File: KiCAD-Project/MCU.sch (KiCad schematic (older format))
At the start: 43 parts, among them J301 GPIOs, J302 JTAG/SW, U301 CY8C6244AZI-S4D92, U302 MCP9700AT-HTT, U303 MCP9700AT-HTT, Y301 32MHz

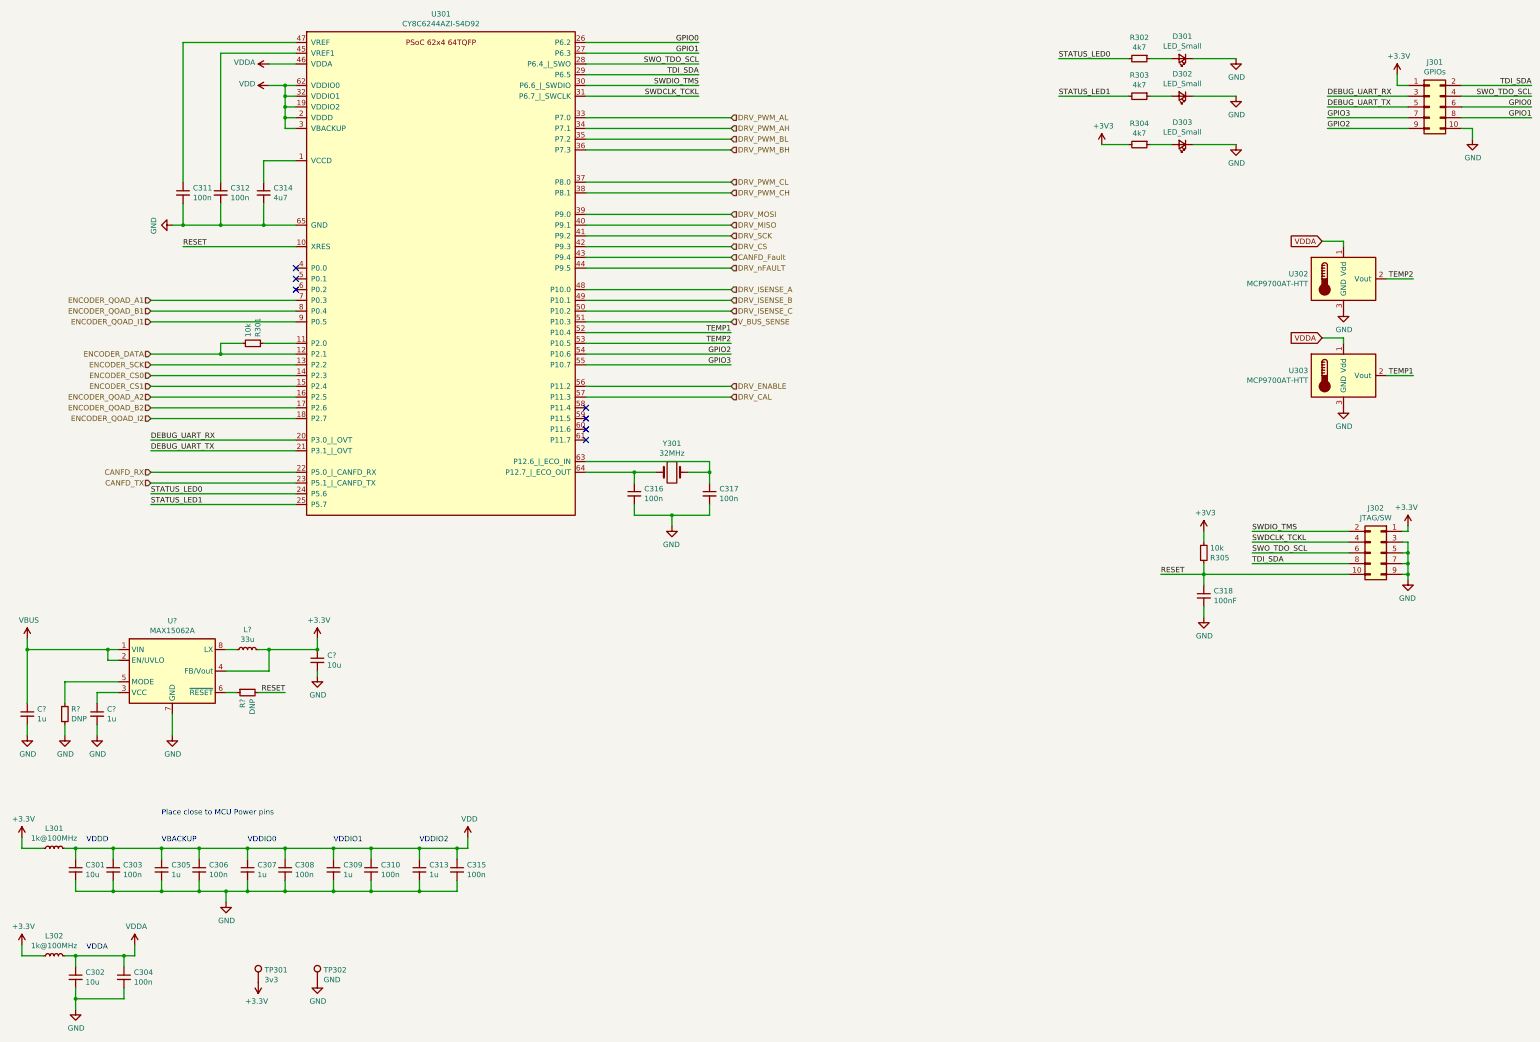
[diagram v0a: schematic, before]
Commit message: Schamtic package assigned
Package assigned, added two 100nF C's for temp sensors
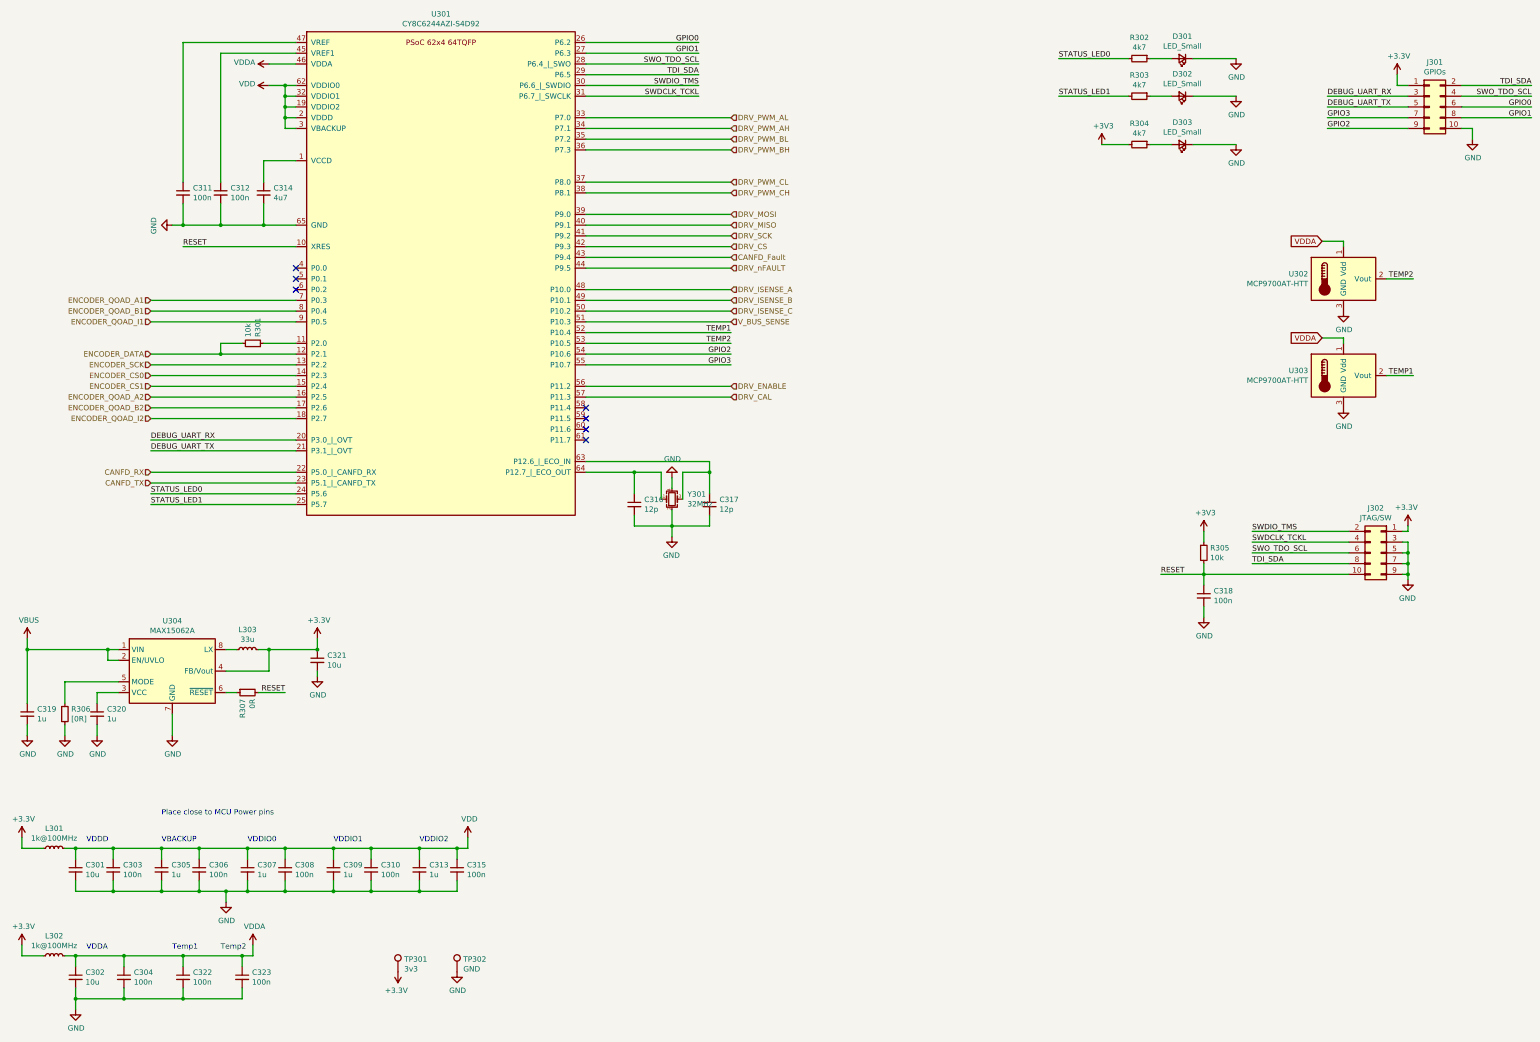
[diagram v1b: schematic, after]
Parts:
- removed Y301: 32MHz, symbol Device:Crystal
- added C322, C323: 100n, Capacitor_SMD:C_0603_1608Metric, symbol Device:C_Small
- added Y301: 32MHz, Crystal:Crystal_SMD_3225-4Pin_3.2x2.5mm_HandSoldering, symbol Device:Crystal_GND24_Small
- C301, C302: footprint (none) -> Capacitor_SMD:C_1206_3216Metric
- C303, C304, C305, C306, C307, C308, C309, C310, C311, C312, C313, C314, C315: footprint (none) -> Capacitor_SMD:C_0603_1608Metric
- C316, C317: value 100n -> 12p; footprint (none) -> Capacitor_SMD:C_0603_1608Metric
- C318: value 100nF -> 100n; footprint (none) -> Capacitor_SMD:C_0603_1608Metric
- C319, C320: renamed from C?; footprint (none) -> Capacitor_SMD:C_0603_1608Metric
- C321: renamed from C?; footprint (none) -> Capacitor_SMD:C_1206_3216Metric
- D301, D302, D303: footprint (none) -> LED_SMD:LED_0603_1608Metric
- J301: footprint (none) -> Connector_PinSocket_2.54mm:PinSocket_2x05_P2.54mm_Vertical
- J302: footprint (none) -> Connector_PinSocket_2.00mm:PinSocket_2x05_P2.00mm_Vertical_SMD
- L301, L302: footprint (none) -> Inductor_SMD:L_0603_1608Metric
- L303: renamed from L?; footprint (none) -> Inductor_SMD:L_1210_3225Metric
- R301, R302, R303, R304, R305: footprint (none) -> Resistor_SMD:R_0603_1608Metric
- R306: renamed from R?; value DNP -> [0R]; footprint (none) -> Resistor_SMD:R_0603_1608Metric
- R307: renamed from R?; value DNP -> 0R; footprint (none) -> Resistor_SMD:R_0603_1608Metric
- TP301: footprint (none) -> TestPoint:TestPoint_Pad_D2.0mm
- TP302: footprint (none) -> Connector_PinHeader_2.54mm:PinHeader_1x01_P2.54mm_Vertical
- U301: footprint (none) -> Package_DFN_QFN:Texas_S-PVQFN-N64_EP4.25x4.25mm_ThermalVias
- gave numbers to parts that had none: 1
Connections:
- net +3V3: now also R305.1; no longer R305.2
- net GND: now also C322.2, C323.2, Y301.2, Y301.4
- net RESET: now also R305.2; no longer R305.1
- net VDDA: now also C322.1, C323.1
- net at C317.1, U301.63 (P12.6_|_ECO_IN): now also Y301.3
- net at C316.1, U301.64 (P12.7_|_ECO_OUT): now also Y301.1
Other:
- note added: "Temp1"
- note added: "Temp2"
- moved on the sheet: C316, C317, TP301, TP302

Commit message: pcb draft
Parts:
- removed C319, C320: 1u, Capacitor_SMD:C_0603_1608Metric, symbol Device:C_Small
- removed C321: 10u, Capacitor_SMD:C_1206_3216Metric, symbol Device:C_Small
- removed L303: 33u, Inductor_SMD:L_1210_3225Metric, symbol Device:L_Small
- removed U304: MAX15062A, Package_DFN_QFN:DFN-8_2x2mm_P0.5mm, symbol Regulator_Switching:MAX15062A
- J301: footprint Connector_PinSocket_2.54mm:PinSocket_2x05_P2.54mm_Vertical -> Connector_PinHeader_2.54mm:PinHeader_2x05_P2.54mm_Vertical_SMD
- J302: footprint Connector_PinSocket_2.00mm:PinSocket_2x05_P2.00mm_Vertical_SMD -> Connector_PinHeader_2.00mm:PinHeader_2x05_P2.00mm_Vertical_SMD
- R306: value [0R] -> 4k7
- R307: value 0R -> 4k7
- Y301: footprint Crystal:Crystal_SMD_3225-4Pin_3.2x2.5mm_HandSoldering -> Crystal:Crystal_SMD_3225-4Pin_3.2x2.5mm
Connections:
- net +3V3: now also R306.1, R307.1
- net DEBUG_UART_RX: now also J301.7 (Pin_7); no longer J301.3 (Pin_3)
- net DEBUG_UART_TX: now also J301.9 (Pin_9); no longer J301.5 (Pin_5)
- net GND: no longer R306.2
- net GPIO0: now also J301.2 (Pin_2); no longer J301.6 (Pin_6)
- net GPIO1: now also J301.4 (Pin_4); no longer J301.8 (Pin_8)
- net GPIO2: now also J301.5 (Pin_5); no longer J301.9 (Pin_9)
- net GPIO3: now also J301.3 (Pin_3); no longer J301.7 (Pin_7)
- net RESET: no longer R307.2
- net SWO_TDO_SCL: now also J301.6 (Pin_6), R306.2; no longer J301.4 (Pin_4)
- net TDI_SDA: now also J301.8 (Pin_8), R307.2; no longer J301.2 (Pin_2)
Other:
- moved on the sheet: J301, U302, U303

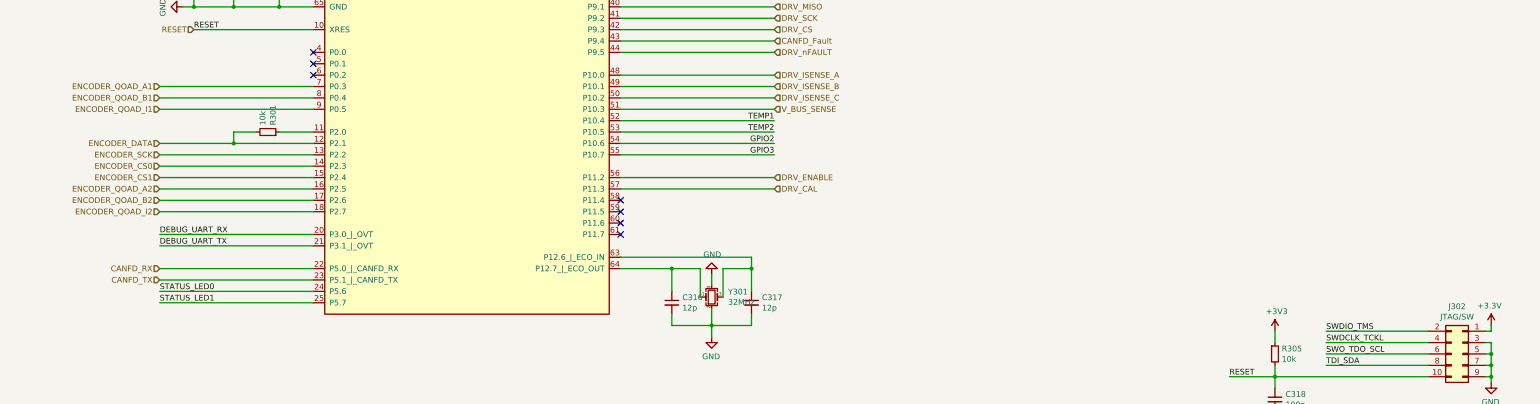
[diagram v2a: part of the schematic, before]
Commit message: layout redesign started
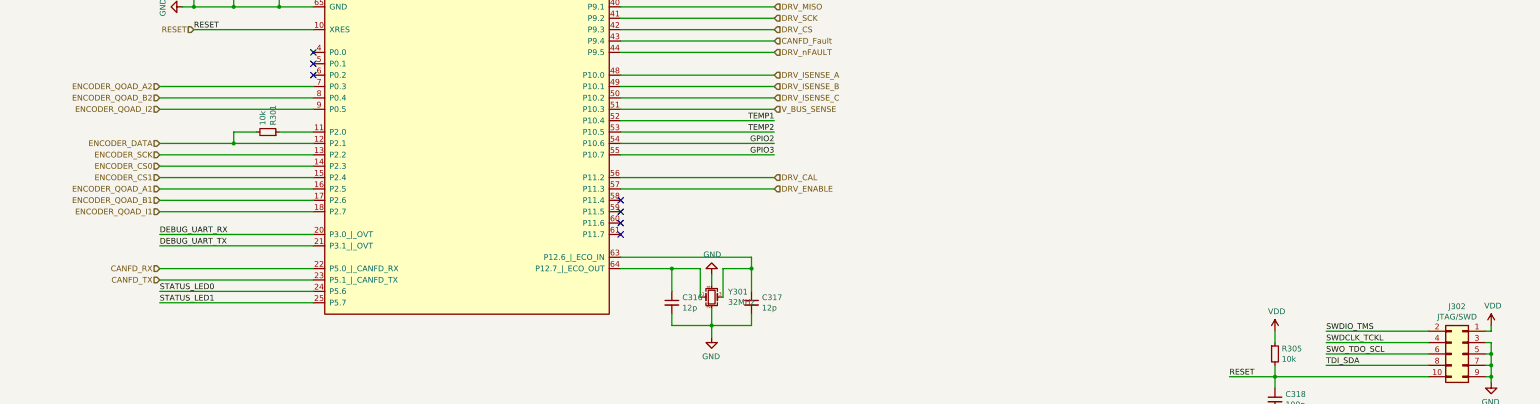
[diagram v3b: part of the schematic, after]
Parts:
- C301, C302: footprint Capacitor_SMD:C_1206_3216Metric -> Capacitor_SMD:C_0603_1608Metric
- J302: value JTAG/SW -> JTAG/SWD; footprint Connector_PinHeader_2.00mm:PinHeader_2x05_P2.00mm_Vertical_SMD -> Connector_PinHeader_1.27mm:PinHeader_2x05_P1.27mm_Vertical_SMD
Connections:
- net +3V3: no longer J302.1 (Pin_1), R305.1
- net DRV_CAL: now also U301.56 (P11.2); no longer U301.57 (P11.3)
- net DRV_ENABLE: now also U301.57 (P11.3); no longer U301.56 (P11.2)
- net ENCODER_QOAD_A1: now also U301.16 (P2.5); no longer U301.7 (P0.3)
- net ENCODER_QOAD_A2: now also U301.7 (P0.3); no longer U301.16 (P2.5)
- net ENCODER_QOAD_B1: now also U301.17 (P2.6); no longer U301.8 (P0.4)
- net ENCODER_QOAD_B2: now also U301.8 (P0.4); no longer U301.17 (P2.6)
- net ENCODER_QOAD_I1: now also U301.18 (P2.7); no longer U301.9 (P0.5)
- net ENCODER_QOAD_I2: now also U301.9 (P0.5); no longer U301.18 (P2.7)
- net VDD: now also J302.1 (Pin_1), R305.1
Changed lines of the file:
@@
 	11600 5950 12000 5950
-$Comp
-L power:+3V3 #PWR?
-U 1 1 60CAF38E
-P 12000 5550
-AR Path="/60CAF38E" Ref="#PWR?"  Part="1"
-AR Path="/60AF747C/60CAF38E" Ref="#PWR0318"  Part="1"
-F 0 "#PWR0318" H 12000 5400 50  0001 C CNN
-F 1 "+3V3" H 12015 5723 50  0000 C CNN
-F 2 "" H 12000 5550 50  0001 C CNN
-F 3 "" H 12000 5550 50  0001 C CNN
-	1    12000 5550
-	1    0    0    -1
-$EndComp
 $Comp
 L power:GND #PWR?
@@
 AR Path="/60AF747C/60CEE033" Ref="J302"  Part="1"
 F 0 "J302" H 13700 6167 50  0000 C CNN
-F 1 "JTAG/SW" H 13700 6076 50  0000 C CNN
-F 2 "Connector_PinHeader_2.00mm:PinHeader_2x05_P2.00mm_Vertical_SMD" H 13650 5750 50  0001 C CNN
+F 1 "JTAG/SWD" H 13700 6076 50  0000 C CNN
+F 2 "Connector_PinHeader_1.27mm:PinHeader_2x05_P1.27mm_Vertical_SMD" H 13650 5750 50  0001 C CNN
 F 3 "~" H 13650 5750 50  0001 C CNN
 	1    13650 5750
-	-1   0    0    -1
-$EndComp
-$Comp
-L power:+3.3V #PWR?
-U 1 1 60CEE03B
-P 13900 5500
-AR Path="/60CEE03B" Ref="#PWR?"  Part="1"
-AR Path="/60AF747C/60CEE03B" Ref="#PWR0323"  Part="1"
-F 0 "#PWR0323" H 13900 5350 50  0001 C CNN
-F 1 "+3.3V" H 13915 5673 50  0000 C CNN
-F 2 "" H 13900 5500 50  0001 C CNN
-F 3 "" H 13900 5500 50  0001 C CNN
-	1    13900 5500
 	-1   0    0    -1
 $EndComp
@@
 Text HLabel 2200 4200 0    50   Input ~ 0
 ENCODER_CS1
+Text HLabel 2200 4300 0    50   Input ~ 0
+ENCODER_QOAD_A1
+Text HLabel 2200 4400 0    50   Input ~ 0
+ENCODER_QOAD_B1
+Text HLabel 2200 4500 0    50   Input ~ 0
+ENCODER_QOAD_I1
 Text HLabel 2200 3400 0    50   Input ~ 0
-ENCODER_QOAD_A1
+ENCODER_QOAD_A2
 Text HLabel 2200 3500 0    50   Input ~ 0
-ENCODER_QOAD_B1
+ENCODER_QOAD_B2
 Text HLabel 2200 3600 0    50   Input ~ 0
-ENCODER_QOAD_I1
-Text HLabel 2200 4300 0    50   Input ~ 0
-ENCODER_QOAD_A2
-Text HLabel 2200 4400 0    50   Input ~ 0
-ENCODER_QOAD_B2
-Text HLabel 2200 4500 0    50   Input ~ 0
 ENCODER_QOAD_I2
 Text HLabel 7600 1700 2    50   Input ~ 0
@@
 Text HLabel 7600 2400 2    50   Input ~ 0
 DRV_PWM_CH
+Text HLabel 7600 4200 2    50   Input ~ 0
+DRV_CAL
 Text HLabel 7600 4300 2    50   Input ~ 0
-DRV_CAL
-Text HLabel 7600 4200 2    50   Input ~ 0
 DRV_ENABLE
 Text HLabel 7600 3100 2    50   Input ~ 0
@@
 F 0 "C302" H 1592 9746 50  0000 L CNN
 F 1 "10u" H 1592 9655 50  0000 L CNN
-F 2 "Capacitor_SMD:C_1206_3216Metric" H 1500 9700 50  0001 C CNN
+F 2 "Capacitor_SMD:C_0603_1608Metric" H 1500 9700 50  0001 C CNN
 F 3 "~" H 1500 9700 50  0001 C CNN
 	1    1500 9700
@@
 F 0 "C301" H 1592 8746 50  0000 L CNN
 F 1 "10u" H 1592 8655 50  0000 L CNN
-F 2 "Capacitor_SMD:C_1206_3216Metric" H 1500 8700 50  0001 C CNN
+F 2 "Capacitor_SMD:C_0603_1608Metric" H 1500 8700 50  0001 C CNN
 F 3 "~" H 1500 8700 50  0001 C CNN
 	1    1500 8700
@@
 Connection ~ 13350 8250
 Connection ~ 13600 8350
+$Comp
+L power:VDD #PWR?
+U 1 1 60CD4D9C
+P 13900 5500
+F 0 "#PWR?" H 13900 5350 50  0001 C CNN
+F 1 "VDD" H 13915 5673 50  0000 C CNN
+F 2 "" H 13900 5500 50  0001 C CNN
+F 3 "" H 13900 5500 50  0001 C CNN
+	1    13900 5500
+	1    0    0    -1
+$EndComp
+$Comp
+L power:VDD #PWR?
+U 1 1 60CE0839
+P 12000 5550
+F 0 "#PWR?" H 12000 5400 50  0001 C CNN
+F 1 "VDD" H 12015 5723 50  0000 C CNN
+F 2 "" H 12000 5550 50  0001 C CNN
+F 3 "" H 12000 5550 50  0001 C CNN
+	1    12000 5550
+	1    0    0    -1
+$EndComp
 $EndSCHEMATC
